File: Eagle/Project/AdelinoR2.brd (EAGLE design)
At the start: 47 x 53.3 mm, 68 parts, among them J1 DC-044-A, J2 YELLOW-8P-2.54, J3 YELLOW-6P-2.54, J4 YELLOW-8P-2.54, J5 YELLOW-8P-2.54, J6 4P-2.0, J7 YELLOW-2X3P-2.54, J8 4P-2.0, Q1 NCE3407A, Q2 CJ2305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

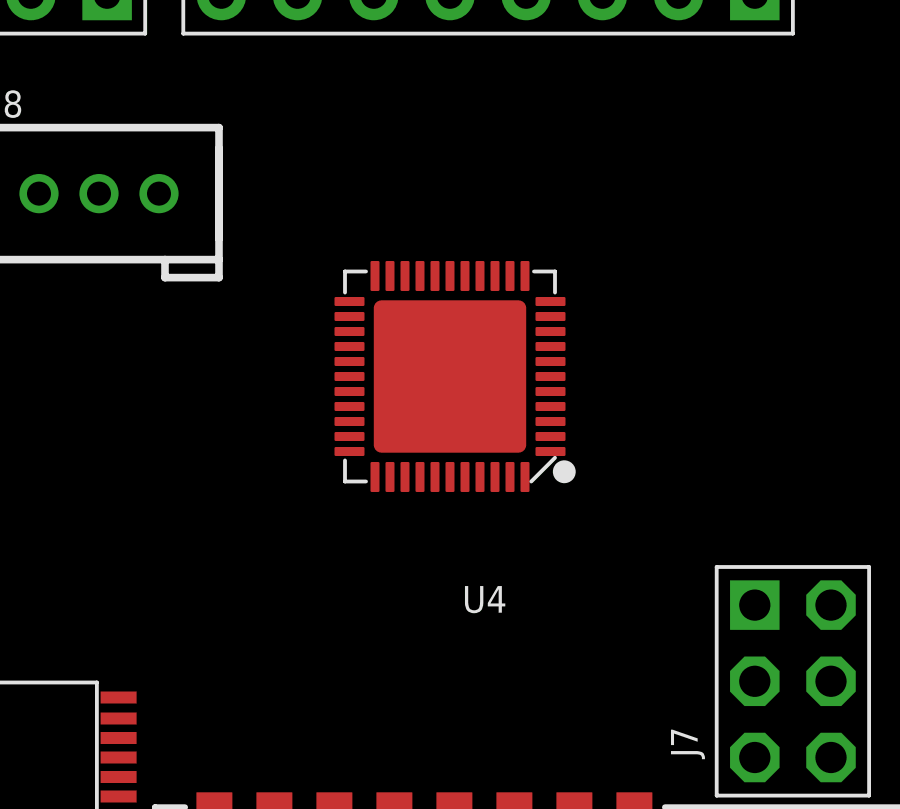
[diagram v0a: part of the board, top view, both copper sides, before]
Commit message: Add alternative TQFP44 socket alongside QFN44.
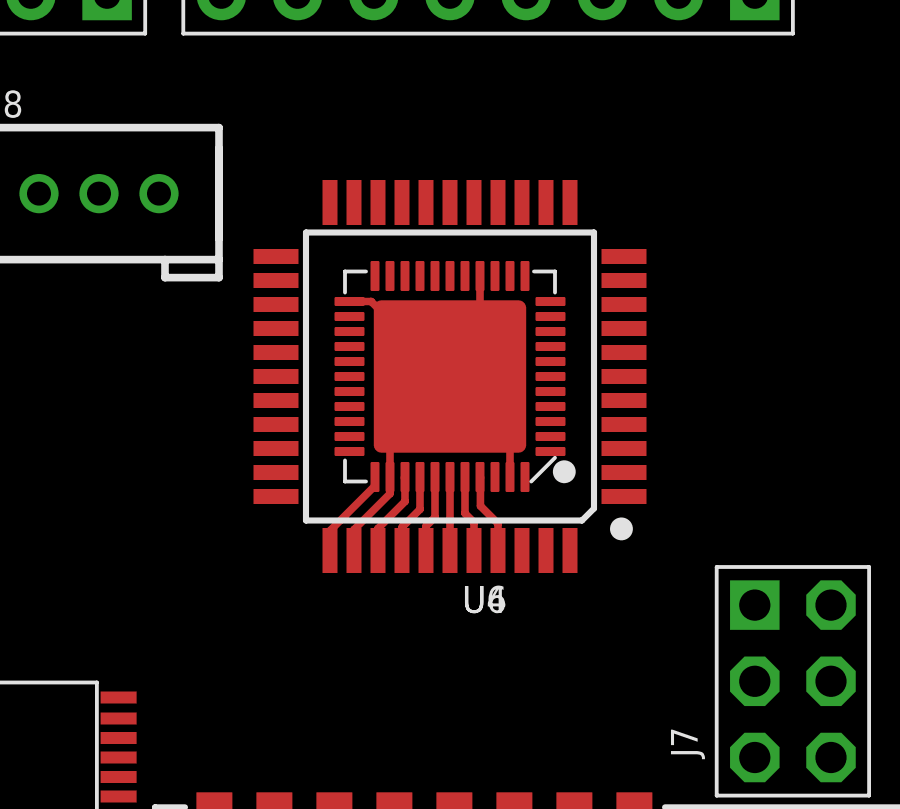
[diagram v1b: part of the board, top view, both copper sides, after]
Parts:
- added U6: ATMEGA32U4-TQFP44, Seeed-IC:TQFP44-0.8-9.6X9.6MM
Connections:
- net +5V: now also U6.34
- net GND: now also U6.35
- net PIN_A0: now also U6.36
- net PIN_A1: now also U6.37
- net PIN_A2: now also U6.38
- net PIN_A3: now also U6.39
- net PIN_A4: now also U6.40
- net PIN_A5: now also U6.41
- net PIN_D13: now also U6.32
- net PIN_D5: now also U6.31
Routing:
- net GND: track 0.00 -> 19.5 mm
- net +5V: track 0.00 -> 3.07 mm
- net PIN_A0: track 0.00 -> 2.86 mm
- net PIN_A5: track 0.00 -> 2.70 mm
- net PIN_A1: track 0.00 -> 2.70 mm
- net PIN_A2: track 0.00 -> 2.59 mm
- net PIN_A4: track 0.00 -> 2.57 mm
- net PIN_A3: track 0.00 -> 2.45 mm

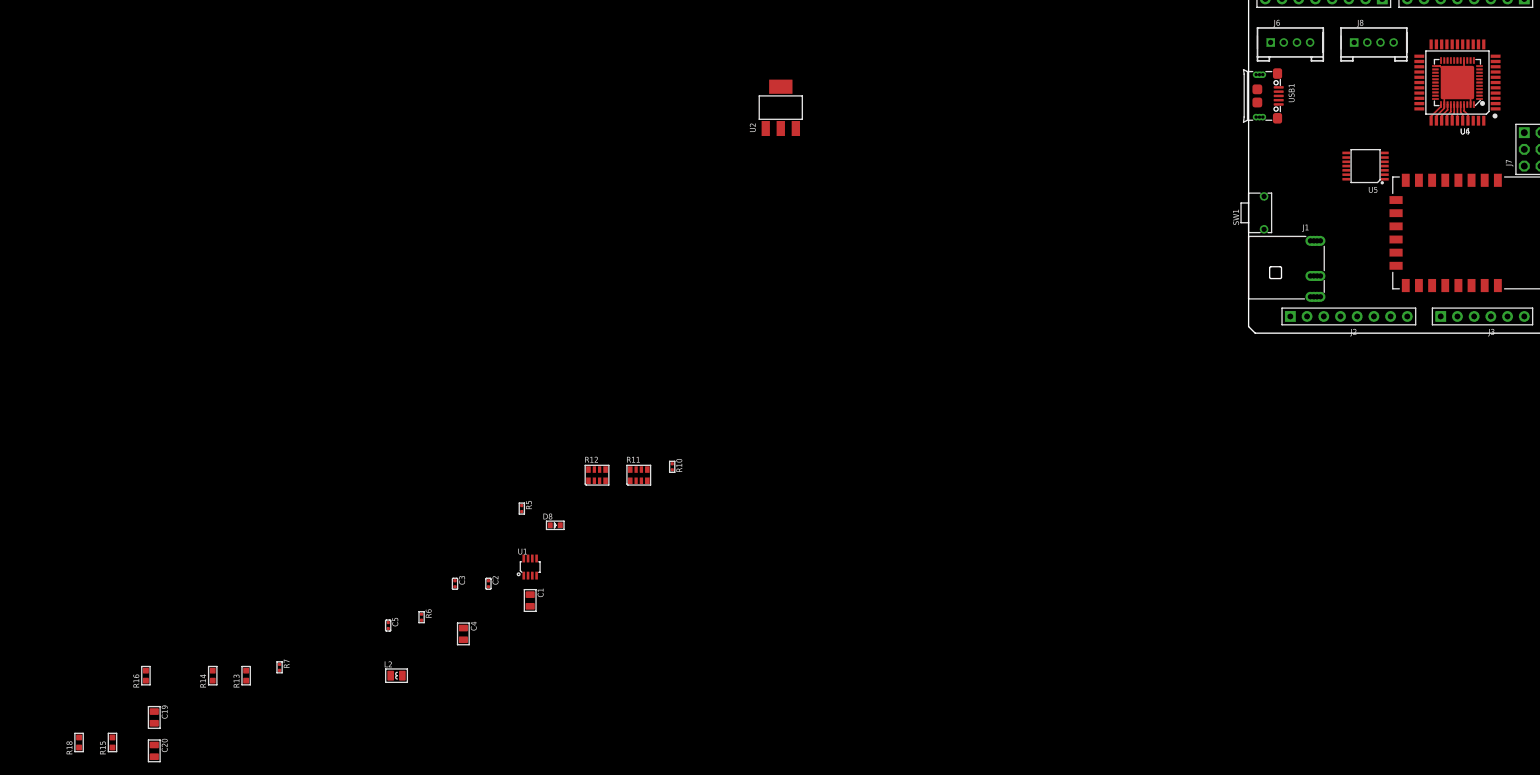
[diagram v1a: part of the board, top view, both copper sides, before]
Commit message: Getting proper double-socket pairing; minor tweaks.
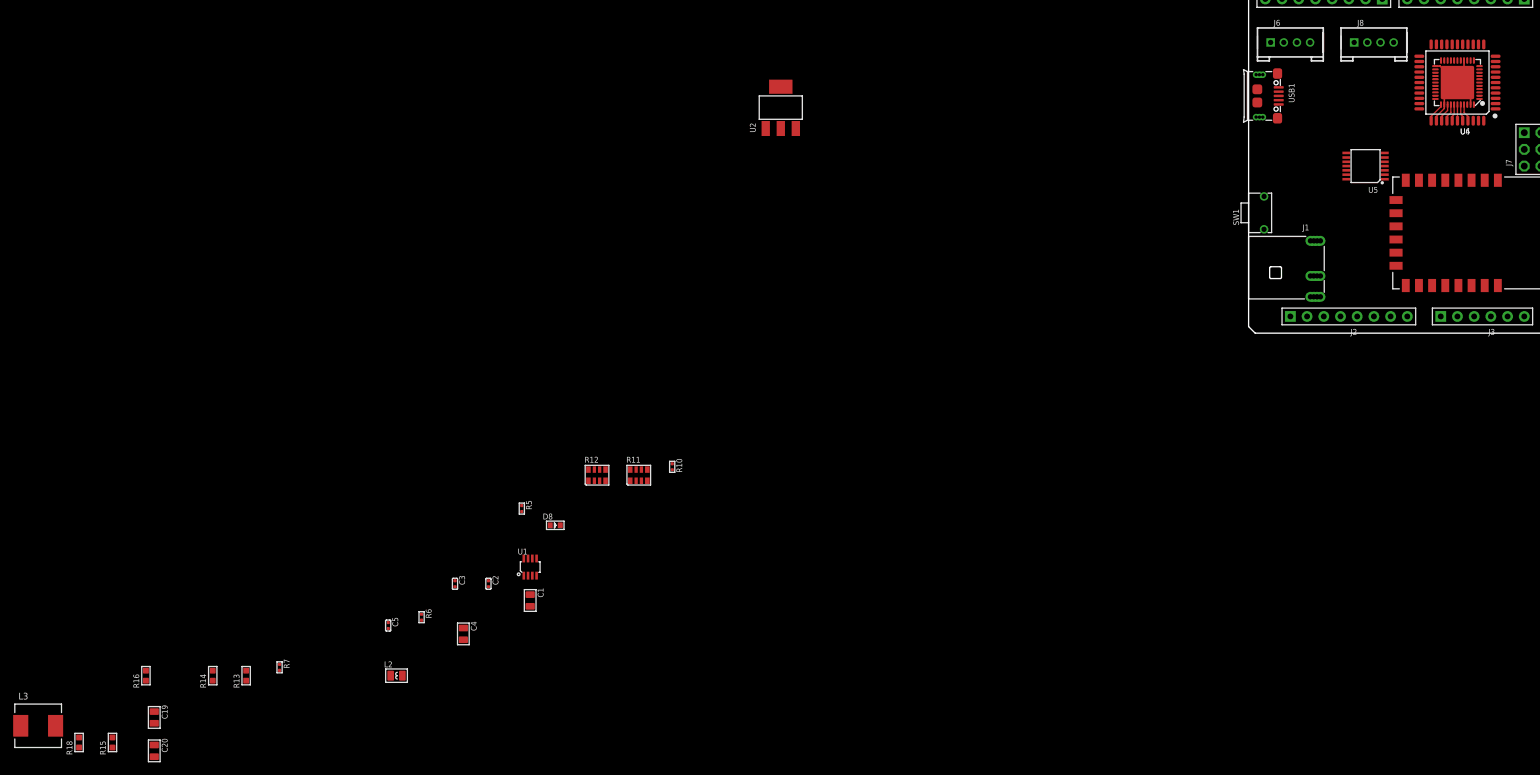
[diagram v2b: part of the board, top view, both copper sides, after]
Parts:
- added L3: 303010525_22UH_7.1X6.6MM, Seeed-OPL-2017-01-Inductor-Akita:L2826

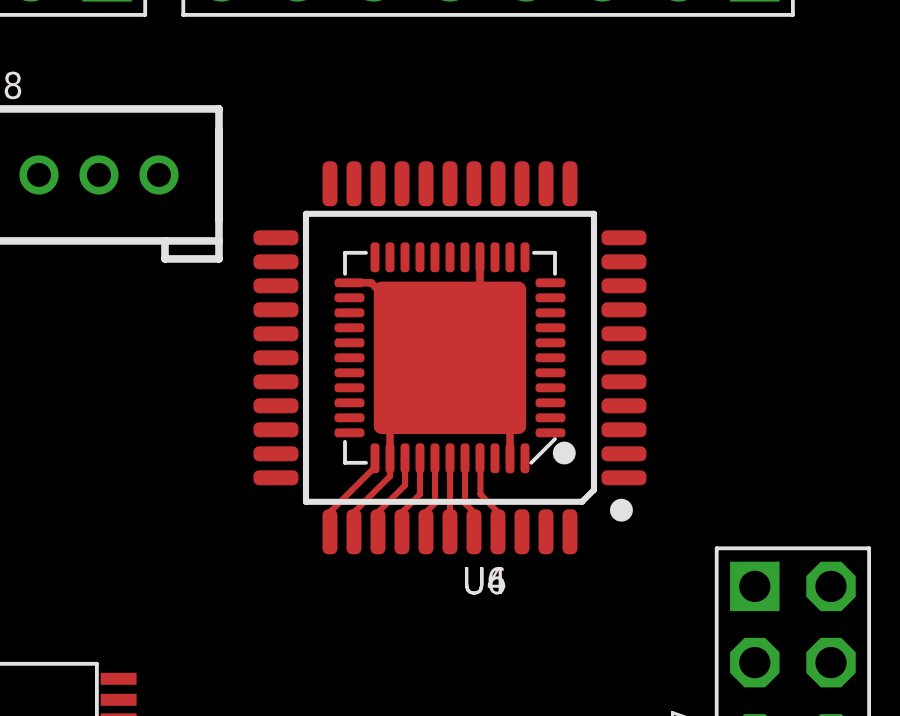
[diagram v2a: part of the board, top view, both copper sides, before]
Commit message: Double socket TQFP44+QFN44 finished.
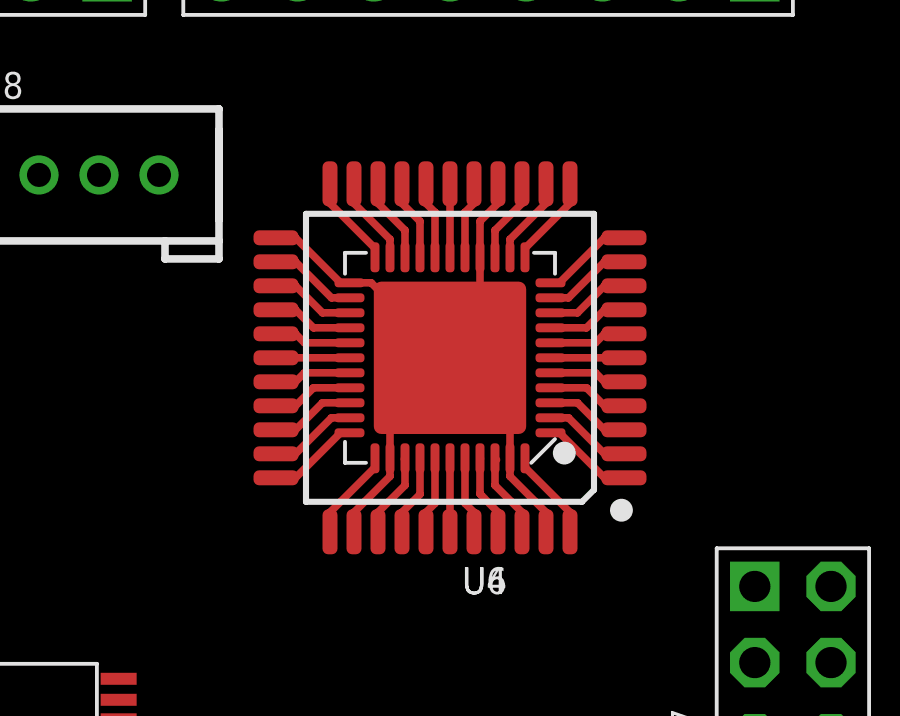
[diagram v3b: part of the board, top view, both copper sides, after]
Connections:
- removed net N$7: C16.2, U4.6
- new net UCAP: C16.2, U4.6, U6.6
- net +5V: now also U6.14, U6.24, U6.44
- net ACT_LED: now also U6.8
- net D+: now also U6.4
- net D-: now also U6.3
- net ESP_EN: now also U6.22
- net GND: now also U6.15, U6.23, U6.43
- net MISO: now also U6.11
- net MOSI: now also U6.10
- net PIN_AREF: now also U6.42
- net PIN_D0: now also U6.20
- net PIN_D1: now also U6.21
- net PIN_D10: now also U6.30
- net PIN_D11: now also U6.12
- net PIN_D12: now also U6.26
- net PIN_D2: now also U6.19
- net PIN_D3: now also U6.18
- net PIN_D4: now also U6.25
- net PIN_D6: now also U6.27
- net PIN_D7: now also U6.1
- net PIN_D8: now also U6.28
- net PIN_D9: now also U6.29
- net RESET: now also U6.13
- net RSTAT: now also U6.33
- net SCK: now also U6.9
- net UGND: now also U6.5
- net VUSB: now also U6.2, U6.7
- net XTAL1: now also U6.17
- net XTAL2: now also U6.16
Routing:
- net +5V: track 3.07 -> 11.9 mm
- net GND: track 19.5 -> 28.2 mm
- net VUSB: track 0.00 -> 5.52 mm
- net RSTAT: track 0.00 -> 3.07 mm
- net PIN_D7: track 0.00 -> 3.07 mm
- net PIN_D11: track 0.00 -> 3.07 mm
- net MISO: track 0.00 -> 3.07 mm
- net ESP_EN: track 0.00 -> 3.07 mm
- net PIN_D13: track 0.00 -> 2.95 mm
- net RESET: track 0.00 -> 2.95 mm
- net PIN_D1: track 0.00 -> 2.95 mm
- net MOSI: track 0.00 -> 2.95 mm
- net PIN_AREF: track 0.00 -> 2.89 mm
- net PIN_D5: track 0.00 -> 2.82 mm
- net PIN_D4: track 0.00 -> 2.82 mm
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
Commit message: Power supply routing wip.
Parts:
- removed L3: 303010525_22UH_7.1X6.6MM, Seeed-OPL-2017-01-Inductor-Akita:L2826
- removed R14: 10K / 1%, Seeed-Resistor:R0603
- removed R16: 30K / 1%, Seeed-Resistor:R0603
- L2: device Seeed-Inductor:L0806 -> Seeed-Inductor:L5040S
- R13: value 68K / 1% -> 2K7 / 1%
- R18: value 3K / 1% -> 3.3K; device Seeed-Resistor:R0603 -> Seeed-Resistor:R0402
- moved R18 207.6 mm to (16.9, 9.91), turned to 90 degrees
- moved R15 206.4 mm to (19.9, 11.9)
- moved C20 201.4 mm to (19.2, 14.9), turned to 270 degrees
- moved C19 200.3 mm to (19.2, 17.1), turned to 270 degrees
- moved R13 182.4 mm to (18.4, 11.9), turned to 180 degrees
- moved R7 171.5 mm to (13.5, 8.89), turned to 270 degrees
- moved L2 159.4 mm to (14.2, 16.8), turned to 180 degrees
- moved C5 159.0 mm to (16.9, 14.3)
- moved R6 152.7 mm to (16.9, 11.3), turned to 180 degrees
- moved C4 147.3 mm to (18.3, 6.60), turned to 180 degrees
- moved R5 145.8 mm to (25.1, 26.9)
- moved D8 144.5 mm to (32.8, 13.2), turned to 90 degrees
- moved C2 142.7 mm to (19.2, 8.89), turned to 270 degrees
- moved C3 142.6 mm to (12.6, 12.7)
- moved R11 136.9 mm to (38.4, 18.0)
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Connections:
- net N$10 renamed SW_VCC_IN
- net N$12 renamed SW_VCAP
- net N$14 renamed SW_BS
- net N$19 renamed SW_VCC_OUT
- net N$20 renamed SW_EN
- net N$24 renamed SW_FB
- net N$4 renamed SW_SS
- removed net N$21: R16.1, R18.2
- removed net N$22: R14.1, R15.2
- net N$23: now also R15.2, R18.2; no longer R14.2, R16.2
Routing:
- net GND: track 28.2 -> 74.9 mm
- net VIN: track 0.00 -> 16.4 mm
- net SW_VCC_IN: track 0.00 -> 11.7 mm
- net SW_SS: track 0.00 -> 10.0 mm, vias 0 -> 2
- net +5V: track 11.9 -> 21.2 mm
- net +3V3: track 0.00 -> 6.35 mm
- net SW_VCAP: track 0.00 -> 4.80 mm
- net SW_VCC_OUT: track 0.00 -> 4.53 mm
- net SW_BS: track 0.00 -> 4.10 mm
- net N$23: track 0.00 -> 3.23 mm
- net N$15: track 0.00 -> 2.57 mm
- net SW_EN: track 0.00 -> 1.57 mm
- net SW_FB: track 0.00 -> 0.87 mm

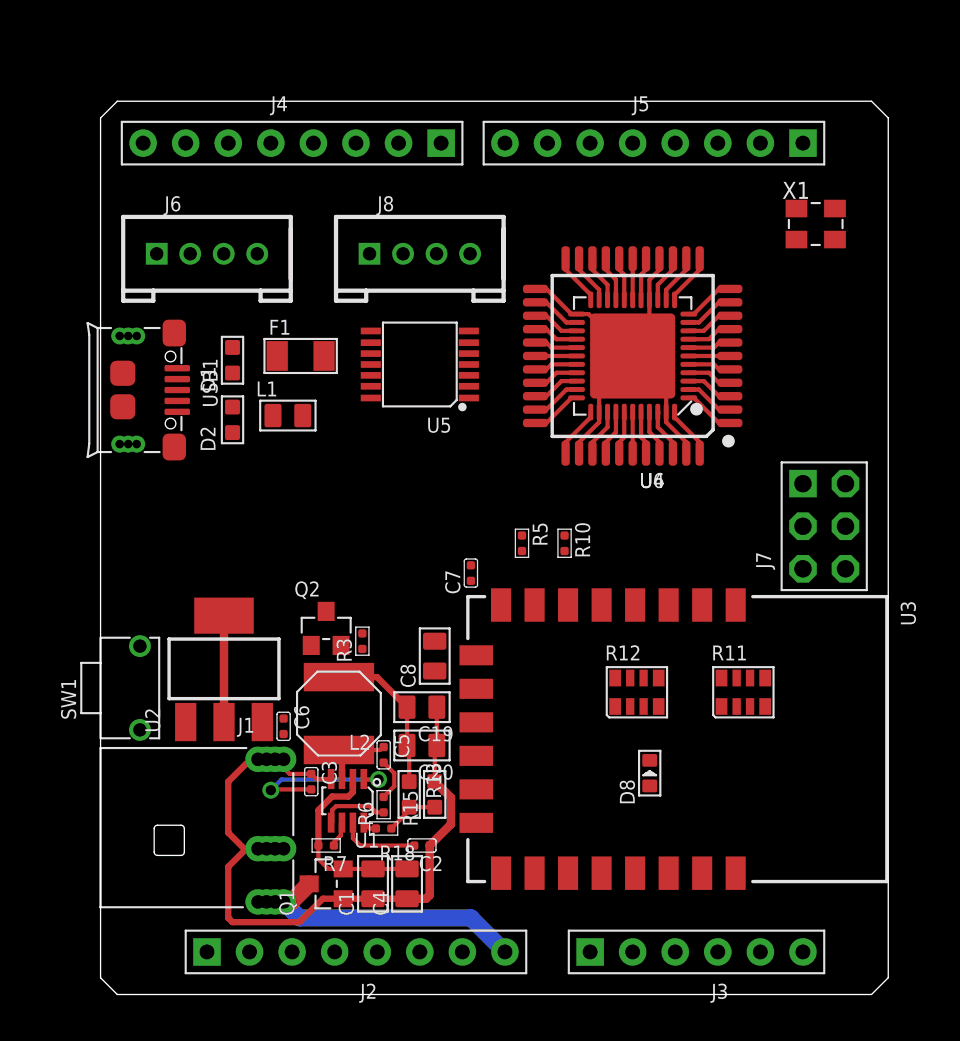
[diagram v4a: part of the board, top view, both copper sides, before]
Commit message: Add TVS to protect power input.
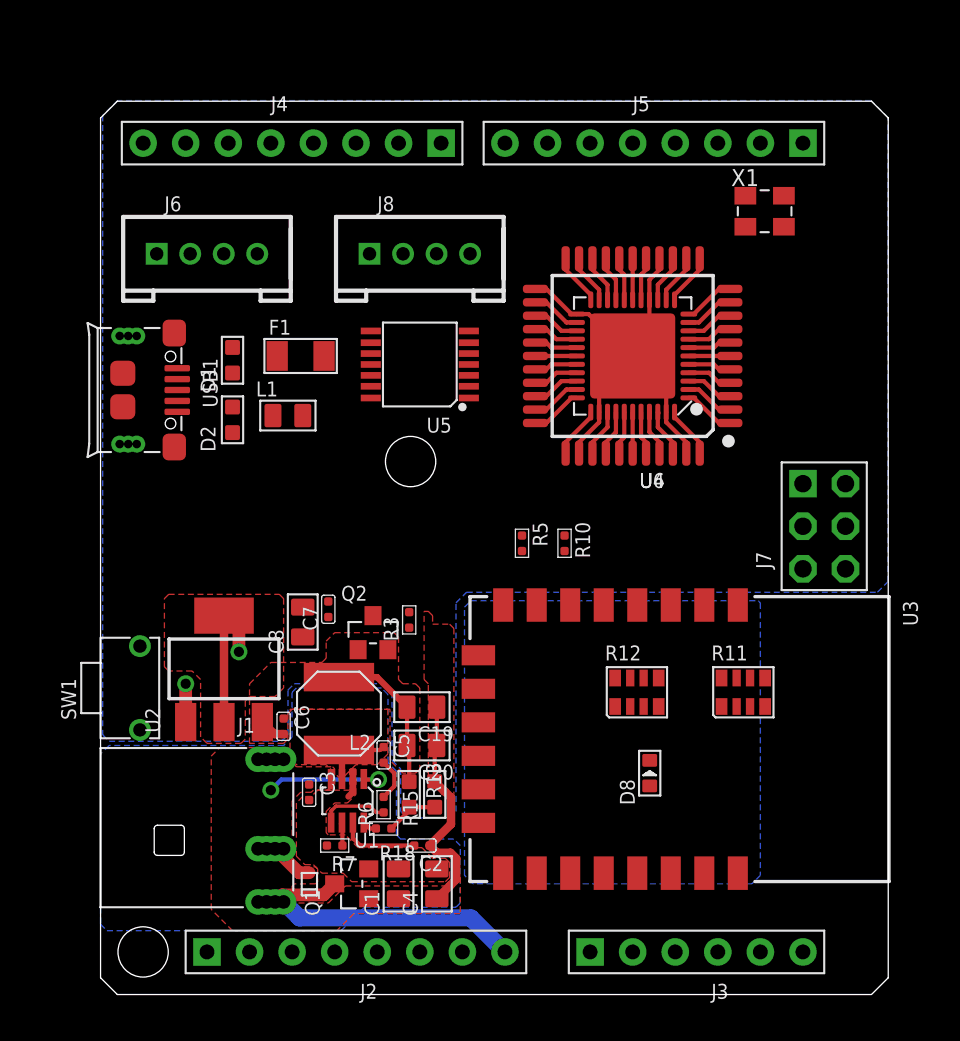
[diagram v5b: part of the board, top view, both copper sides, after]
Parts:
- added TVS1: (no value), Seeed-OPL-2017-01-Diode-james:SOD-523
- moved C7 8.78 mm to (13.6, 23.0)
- moved C8 8.13 mm to (12.1, 22.2)
- moved X1 3.14 mm to (39.6, 46.7)
- moved R3 3.07 mm to (18.4, 22.4)
- moved Q2 2.81 mm to (16.3, 21.6)
- moved C4 1.78 mm to (20.1, 6.60)
- moved C1 1.52 mm to (17.8, 6.60)
- moved Q1 1.52 mm to (15.0, 6.60)
- moved C3 0.65 mm to (12.4, 12.1)
- moved R7 0.51 mm to (14.0, 8.89)
- moved U3 0.13 mm to (34.5, 15.2)
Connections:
- net D+: now also R2.2; no longer R1.2
- net D-: now also R1.2; no longer R2.2
- net GND: now also TVS1.P$1
- net VIN: now also TVS1.P$2
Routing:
- net GND: track 74.9 -> 52.2 mm, vias 0 -> 1
- net SW_VCC_IN: track 11.7 -> 1.15 mm
- net +3V3: track 6.35 -> 8.88 mm, vias 0 -> 1
- net SW_SS: track 10.0 -> 7.58 mm
- net VIN: track 16.4 -> 18.4 mm
- net +5V: track 21.2 -> 22.8 mm
- added copper zone on layer 1, net +3V3
- added copper zone on layer 1, net +5V
- added copper zone on layer 1, net GND
- added copper zone on layer 16, net GND
- added copper zone on layer 1, net SW_VCC_IN
- added copper zone on layer 1, net SW_VCC_OUT
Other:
- outline, holes or cut-outs redrawn

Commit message: Wip.
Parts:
- added D10, D9: YEL-0603, Seeed-LED:LED-0603
- added D11: 20V-500MA, Seeed-Diode:SOD-123
- added D3: GRE-0603, Seeed-LED:LED-0603
- added R14, R16, R21, R22: 1K, Seeed-Resistor:R0402
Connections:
- net MISO renamed AT_MISO
- net MOSI renamed AT_MOSI
- net SCK renamed AT_SCK
- new net AT_SS: U4.8, U6.8
- new net N$10: D10.+, R16.2
- new net N$4: D3.+, R21.2
- new net N$7: D11.+, D9.+, R22.2
- net +5V: now also R21.1
- net ACT_LED: now also R22.1, U4.22, U6.22; no longer U4.8, U6.8
- net BOOT_MODE: now also R14.2
- net ESP_EN: now also U4.33, U6.33; no longer U4.22, U6.22
- net GND: now also D10.-, D3.-, D9.-
- net PIN_D13: now also R14.1, R16.1
- net RSTAT: now also D11.-; no longer U4.33, U6.33
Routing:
- net RSTAT: track 3.07 -> 0.00 mm
- net ESP_EN: track 3.07 -> 0.00 mm
- net ACT_LED: track 2.70 -> 0.00 mm
